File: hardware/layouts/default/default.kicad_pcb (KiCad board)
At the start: 2 copper layers, 20 parts

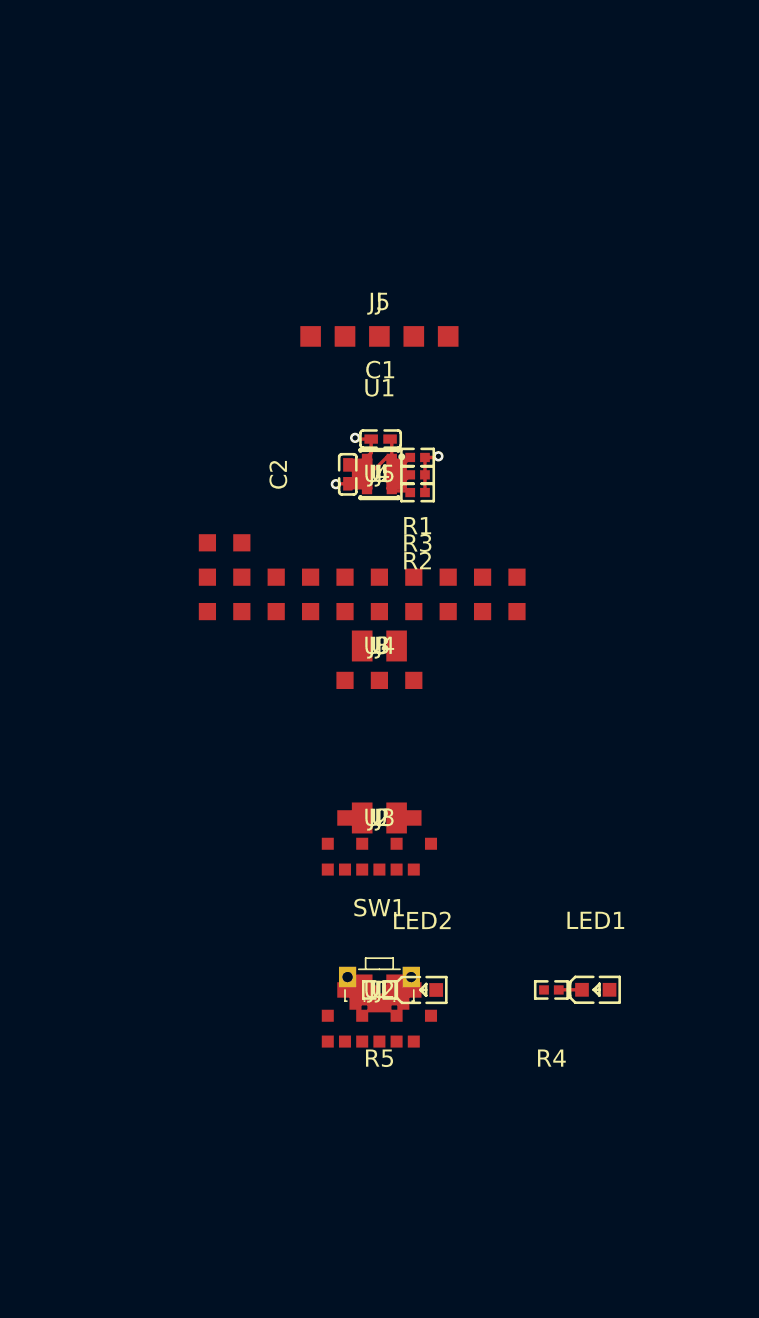
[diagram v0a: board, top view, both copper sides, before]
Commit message: chore(parts): add supplier metadata for AmigoPro (PIM485), Aideepen GPS (Amazon ASIN B08CZSL193), and GY-91; build verified. note: picker doesnt support these suppliers yet. also prep AmigoPro for exact dims per Pimoroni drawing
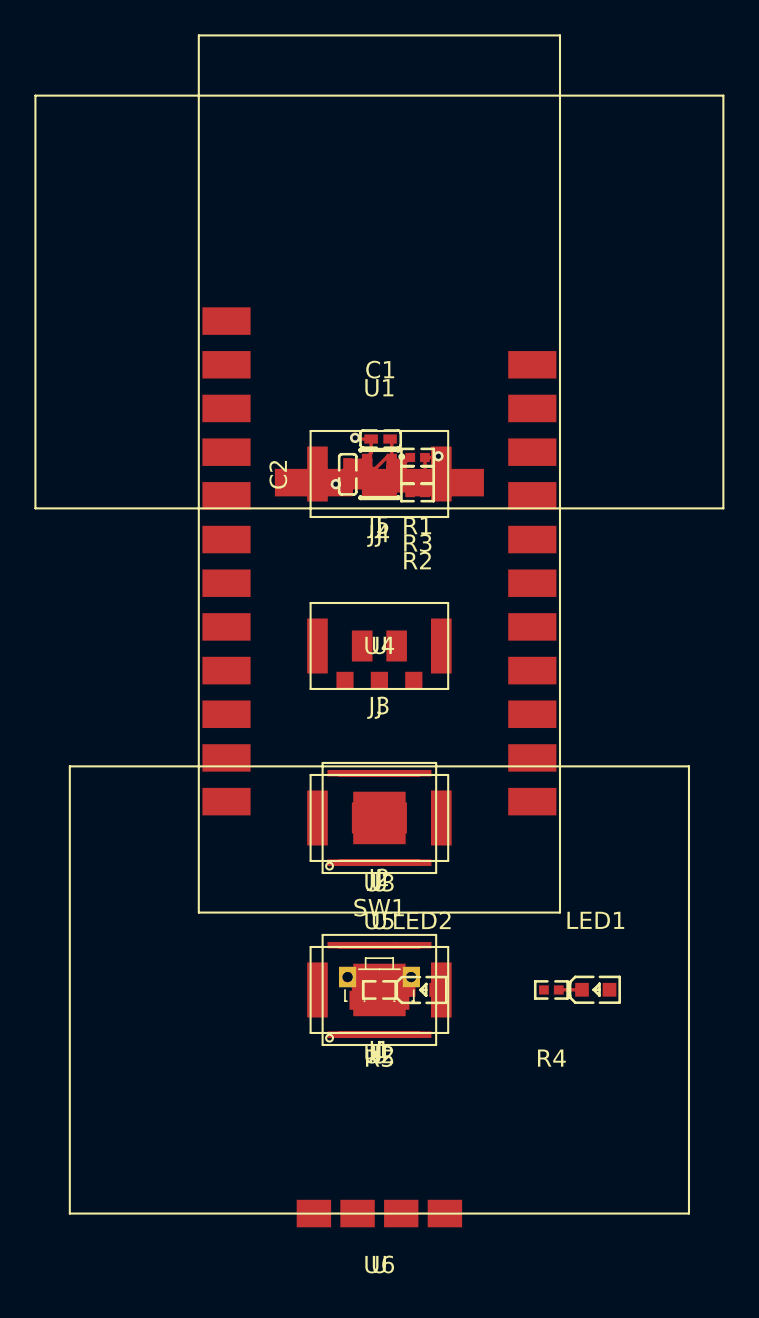
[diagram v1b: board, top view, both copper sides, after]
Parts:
- added U6: , Aideepen_GPS_Module:Aideepen_GPS_Module, F.Cu at (0.00, 0.00)
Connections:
- U5 pad GP0: drv_left-AIN1 -> RX
- U5 pad GP1: drv_left-AIN2 -> TX
- U5 pad GP15: GP15 -> drv_left-SLEEP
- U5 pad GP17: GP17 -> drv_right-SLEEP
- U5 pad GP8: drv_left-SLEEP -> drv_left-AIN1
- U5 pad GP9: drv_right-SLEEP -> drv_left-AIN2
